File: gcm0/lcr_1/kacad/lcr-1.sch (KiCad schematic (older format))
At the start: 122 parts, among them J1 -5V, J10 5V, J11 SWD, J12 -5V, J14 PA3, J15 SPWM, J16 PA9, J17 PA3, J18 PA9, J19 PA6, J2 Hc, J20 PA6, J21 PB1, J22 -5V, J23 5V, J24 3.3, J25 SPWM, J26 1.65V, J27 1.65V, J28 shuai_jian1, J29 shuan_jian, J3 Hp, J30 ADC, J31 +9V, J32 GND, J33 -5V, J34 5V, J35 3.3V, J36 shuai_jian1, J37 shuan_jian, J38 3.3V, J4 Lp, J5 Lc, J6 PB1, J7 5V, J8 5V, J9 ADC, Q1 BC547, Q2 BC547, Q3 BC547, SW1 SW_Push, SW2 SW_Push, U1 NE5532, U10 LM2596S-5, U2 STM32F030F4P6, U3 CD4053B, U4 CD4052B, U5 TL084, U6 LM358, U7 74HC595, U8 LM7805_TO220, U9 LM1117-3.3, Y1 8M

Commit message: PCB
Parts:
- removed C12: 104, Capacitor_THT:C_Disc_D3.0mm_W2.0mm_P2.50mm, symbol Device:C
- added J10: Hc, Connector_Pin:Pin_D1.3mm_L11.0mm_LooseFit, symbol Connector:Conn_01x01_Male
- added J11: Hp, Connector_Pin:Pin_D1.3mm_L11.0mm_LooseFit, symbol Connector:Conn_01x01_Male
- added J6: Lc, Connector_Pin:Pin_D1.3mm_L11.0mm_LooseFit, symbol Connector:Conn_01x01_Male
- added J9: Lp, Connector_Pin:Pin_D1.3mm_L11.0mm_LooseFit, symbol Connector:Conn_01x01_Male
- added R19: 200, Resistor_THT:R_Axial_DIN0204_L3.6mm_D1.6mm_P2.54mm_Vertical, symbol Device:R
- C20: renamed from C29; value 104 -> 105; footprint (none) -> Capacitor_SMD:C_0805_2012Metric_Pad1.18x1.45mm_HandSolder
- R33: renamed from R34; footprint (none) -> Resistor_THT:R_Axial_DIN0204_L3.6mm_D1.6mm_P2.54mm_Vertical
- R34: renamed from R35; footprint (none) -> Resistor_THT:R_Axial_DIN0204_L3.6mm_D1.6mm_P2.54mm_Vertical
- U8: footprint Package_TO_SOT_THT:TO-220-3_Horizontal_TabDown -> Package_TO_SOT_THT:TO-220-3_Vertical
- renumbered C13 to C12, C14 to C13, C15 to C14, C16 to C15, C17 to C16, C18 to C17, C19 to C18, C20 to C19, J38 to J12, J8 to J13, J9 to J14, J10 to J15, J11 to J16, J12 to J17, J14 to J18, J15 to J19, J16 to J20, J17 to J21, J18 to J22, J19 to J23, J20 to J24, J21 to J25, J22 to J26, J23 to J27, J24 to J28, J25 to J29, J26 to J30, J27 to J31, J28 to J32, J29 to J33, J30 to J34, J31 to J35, J32 to J36, J34 to J37, J35 to J38, J36 to J39, J37 to J40, J33 to J41, J6 to J7, J7 to J8, R19 to R20, R20 to R21, R21 to R22, R22 to R23, R23 to R24, R24 to R25, R25 to R26, R26 to R27, R27 to R28, R28 to R29, R29 to R30, R30 to R31, R31 to R32, R32 to R35, R33 to R36
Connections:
- net +9V: now also C20.2
- net -5V: now also R34.1; no longer C20.1
- net GND: no longer R33.2
- net Hc: now also J10.1 (Pin_1)
- net Hp: now also J11.1 (Pin_1)
- net Lc: now also J6.1 (Pin_1)
- net Lp: now also J9.1 (Pin_1)
- net PA4_SPI1_NSS_74HC595_12_RCLK: now also R30.2, U7.12 (RCLK); no longer R31.2, U7.11 (SRCLK)
- net PA5_SPI1_SCK_74HC595_11_SRCLK: now also R31.2, U7.11 (SRCLK); no longer R30.2, U7.12 (RCLK)
- net at C13.1, R16.1, R20.2: now also R19.1
- net at Q3.1 (C): now also R19.2
- new net: C20.1, R33.2
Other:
- moved on the sheet: C20, R33, R34

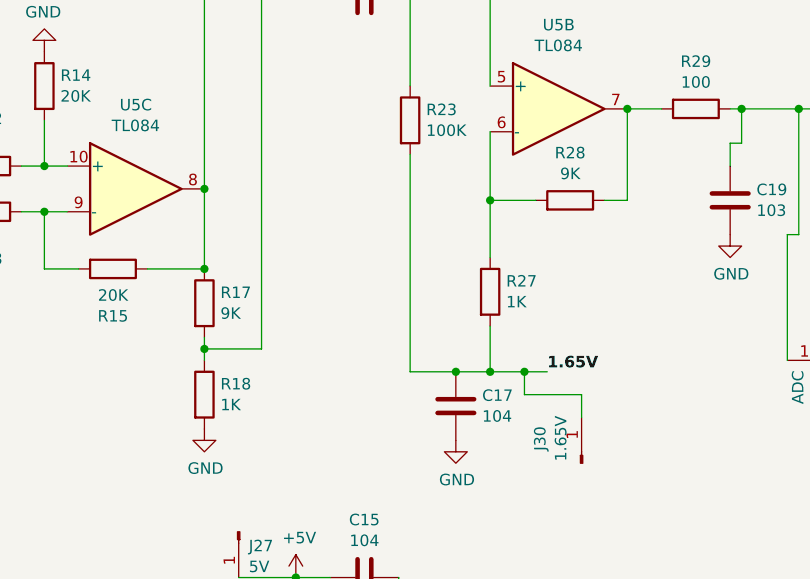
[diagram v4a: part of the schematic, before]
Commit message: 调整档位
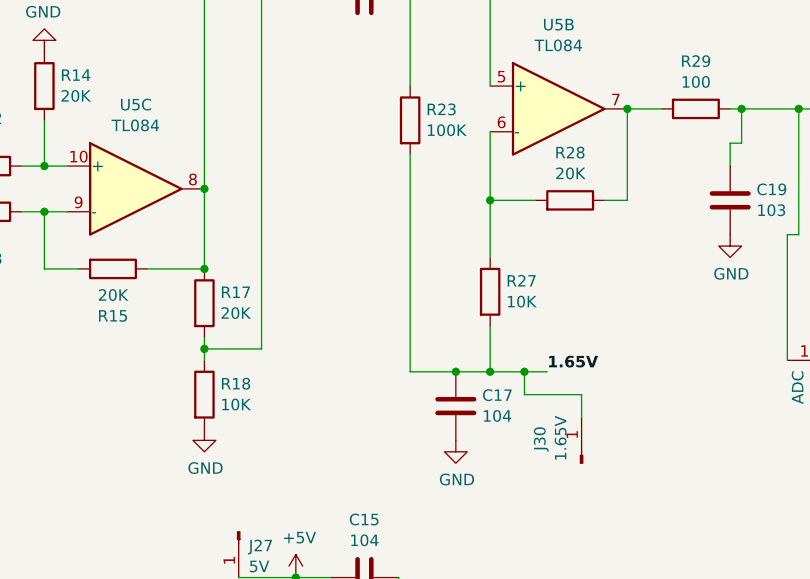
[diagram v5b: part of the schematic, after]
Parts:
- R17, R28: value 9K -> 20K
- R18, R27: value 1K -> 10K
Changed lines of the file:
@@
 P 7650 4350
 F 0 "R28" V 7857 4350 50  0000 C CNN
-F 1 "9K" V 7766 4350 50  0000 C CNN
+F 1 "20K" V 7766 4350 50  0000 C CNN
 F 2 "Resistor_THT:R_Axial_DIN0204_L3.6mm_D1.6mm_P2.54mm_Vertical" V 7580 4350 50  0001 C CNN
 F 3 "~" H 7650 4350 50  0001 C CNN
@@
 P 7300 4750
 F 0 "R27" H 7370 4796 50  0000 L CNN
-F 1 "1K" H 7370 4705 50  0000 L CNN
+F 1 "10K" H 7370 4705 50  0000 L CNN
 F 2 "Resistor_THT:R_Axial_DIN0204_L3.6mm_D1.6mm_P2.54mm_Vertical" V 7230 4750 50  0001 C CNN
 F 3 "~" H 7300 4750 50  0001 C CNN
@@
 P 6050 5200
 F 0 "R18" H 6120 5246 50  0000 L CNN
-F 1 "1K" H 6120 5155 50  0000 L CNN
+F 1 "10K" H 6120 5155 50  0000 L CNN
 F 2 "Resistor_THT:R_Axial_DIN0204_L3.6mm_D1.6mm_P2.54mm_Vertical" V 5980 5200 50  0001 C CNN
 F 3 "~" H 6050 5200 50  0001 C CNN
@@
 P 6050 4800
 F 0 "R17" H 6120 4846 50  0000 L CNN
-F 1 "9K" H 6120 4755 50  0000 L CNN
+F 1 "20K" H 6120 4755 50  0000 L CNN
 F 2 "Resistor_THT:R_Axial_DIN0204_L3.6mm_D1.6mm_P2.54mm_Vertical" V 5980 4800 50  0001 C CNN
 F 3 "~" H 6050 4800 50  0001 C CNN
